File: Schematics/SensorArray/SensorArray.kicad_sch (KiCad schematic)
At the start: 30 parts, among them J1 Conn_01x10_MountingPin, Q1 IRLM2502, Q2 IRLM2502, U1 PCA9557PW, U10 ITR8307, U11 ITR8307, U12 ITR8307, U13 ITR8307, U14 ITR8307, U15 ITR8307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

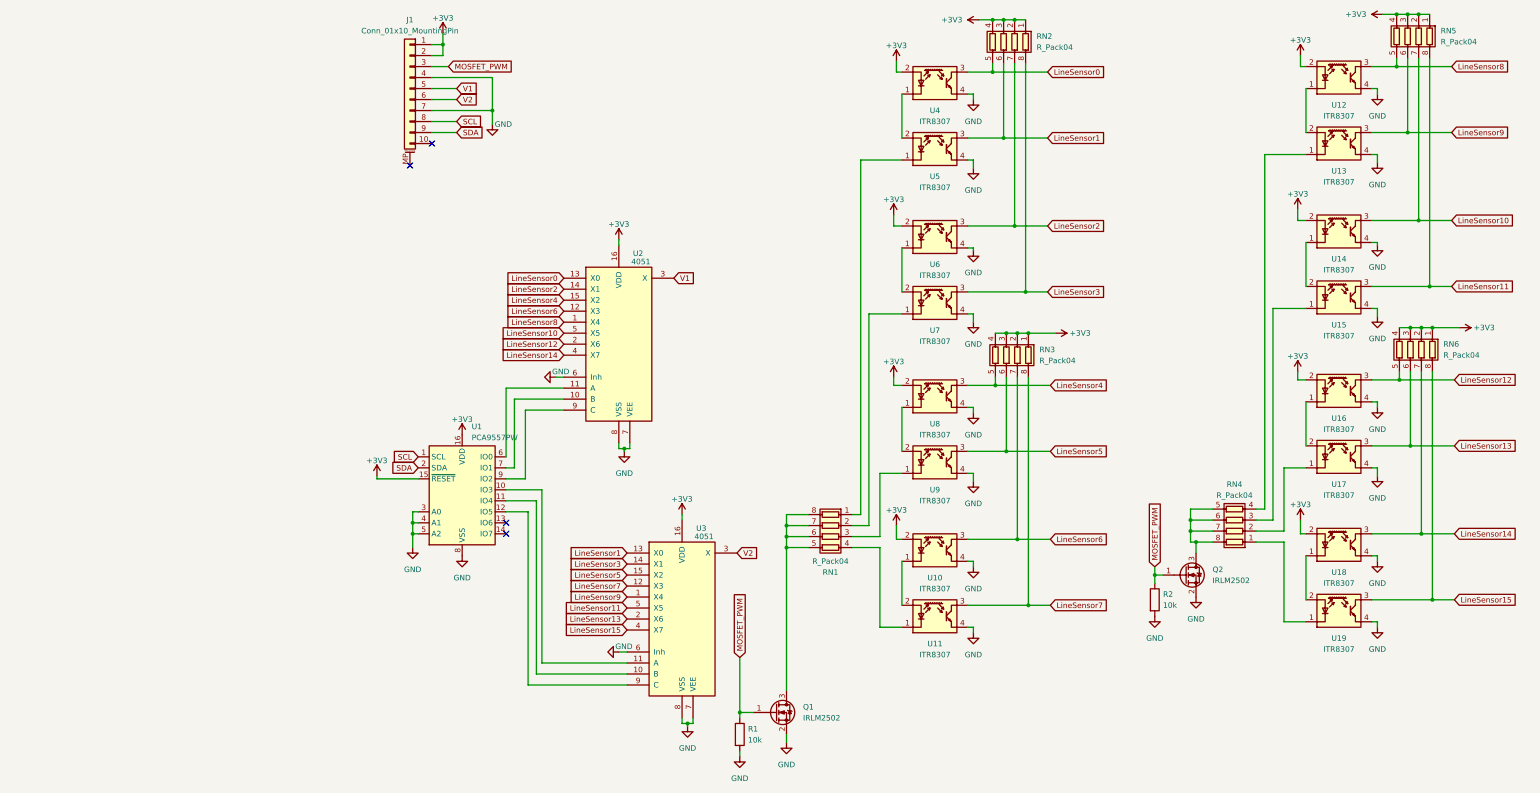
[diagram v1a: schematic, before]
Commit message: Version 1.1 PCB: Fixed I2C pullups
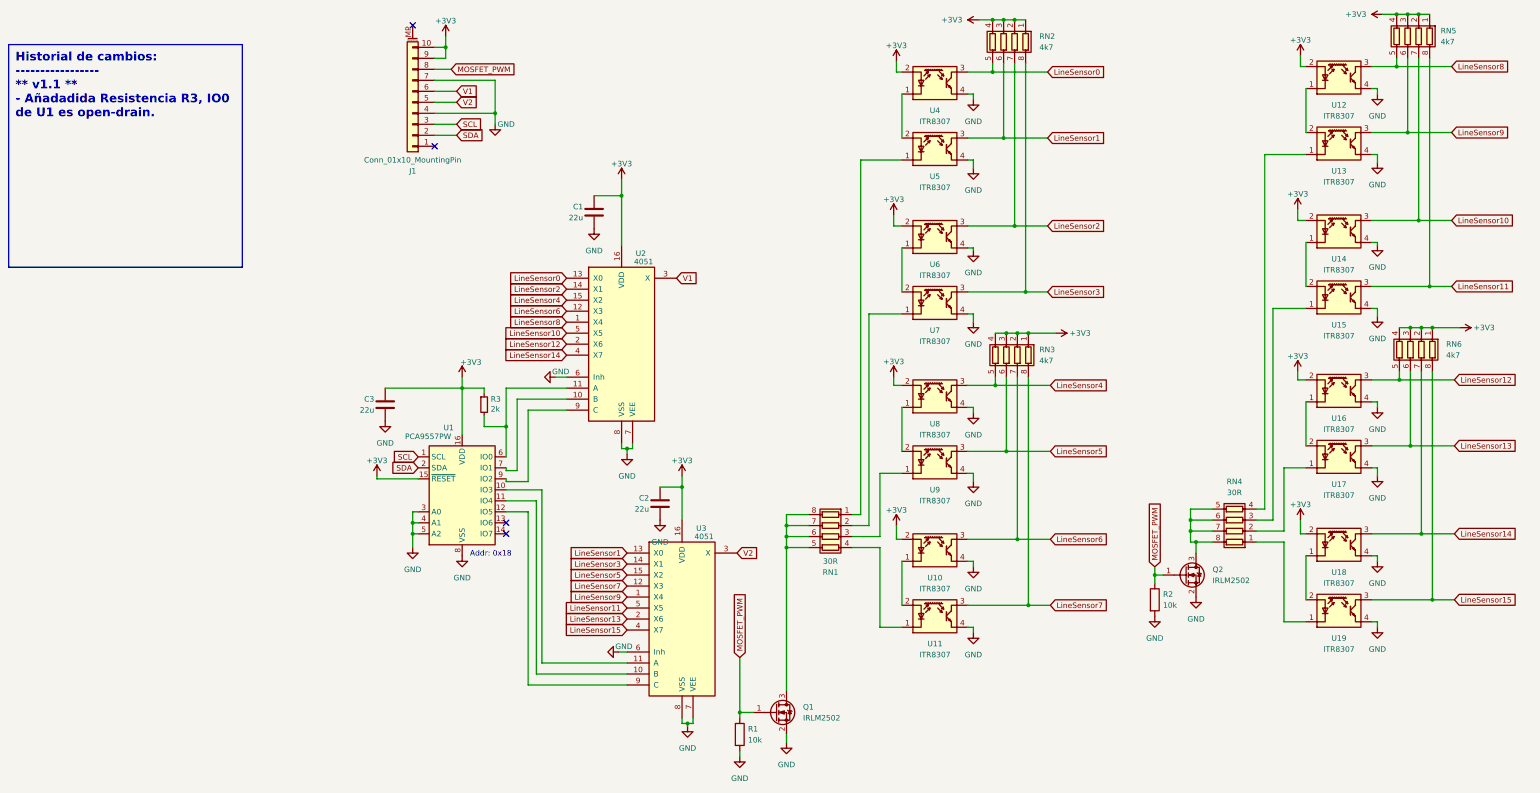
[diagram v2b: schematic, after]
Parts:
- added C1, C2, C3: 22u, Capacitor_SMD:C_0805_2012Metric_Pad1.18x1.45mm_HandSolder, symbol Device:C
- added R3: 2k, symbol Device:R_Small
- RN1, RN4: value R_Pack04 -> 30R
- RN2, RN3, RN5, RN6: value R_Pack04 -> 4k7
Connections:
- net +3V3: now also J1.10 (Pin_10), J1.9 (Pin_9), C1.1, C2.1, C3.1, R3.1; no longer J1.1 (Pin_1), J1.2 (Pin_2)
- net GND: now also C1.2, C2.2, C3.2
- net MOSFET_PWM: now also J1.8 (Pin_8); no longer J1.3 (Pin_3)
- net SCL: now also J1.3 (Pin_3); no longer J1.8 (Pin_8)
- net SDA: now also J1.2 (Pin_2); no longer J1.9 (Pin_9)
- net V1: now also J1.6 (Pin_6); no longer J1.5 (Pin_5)
- net V2: now also J1.5 (Pin_5); no longer J1.6 (Pin_6)
- net at U1.6 (IO0), U2.11 (A): now also R3.2
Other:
- note added: "Addr: 0x18"
- moved on the sheet: J1, U2
